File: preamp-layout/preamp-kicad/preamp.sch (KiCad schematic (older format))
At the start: 15 parts

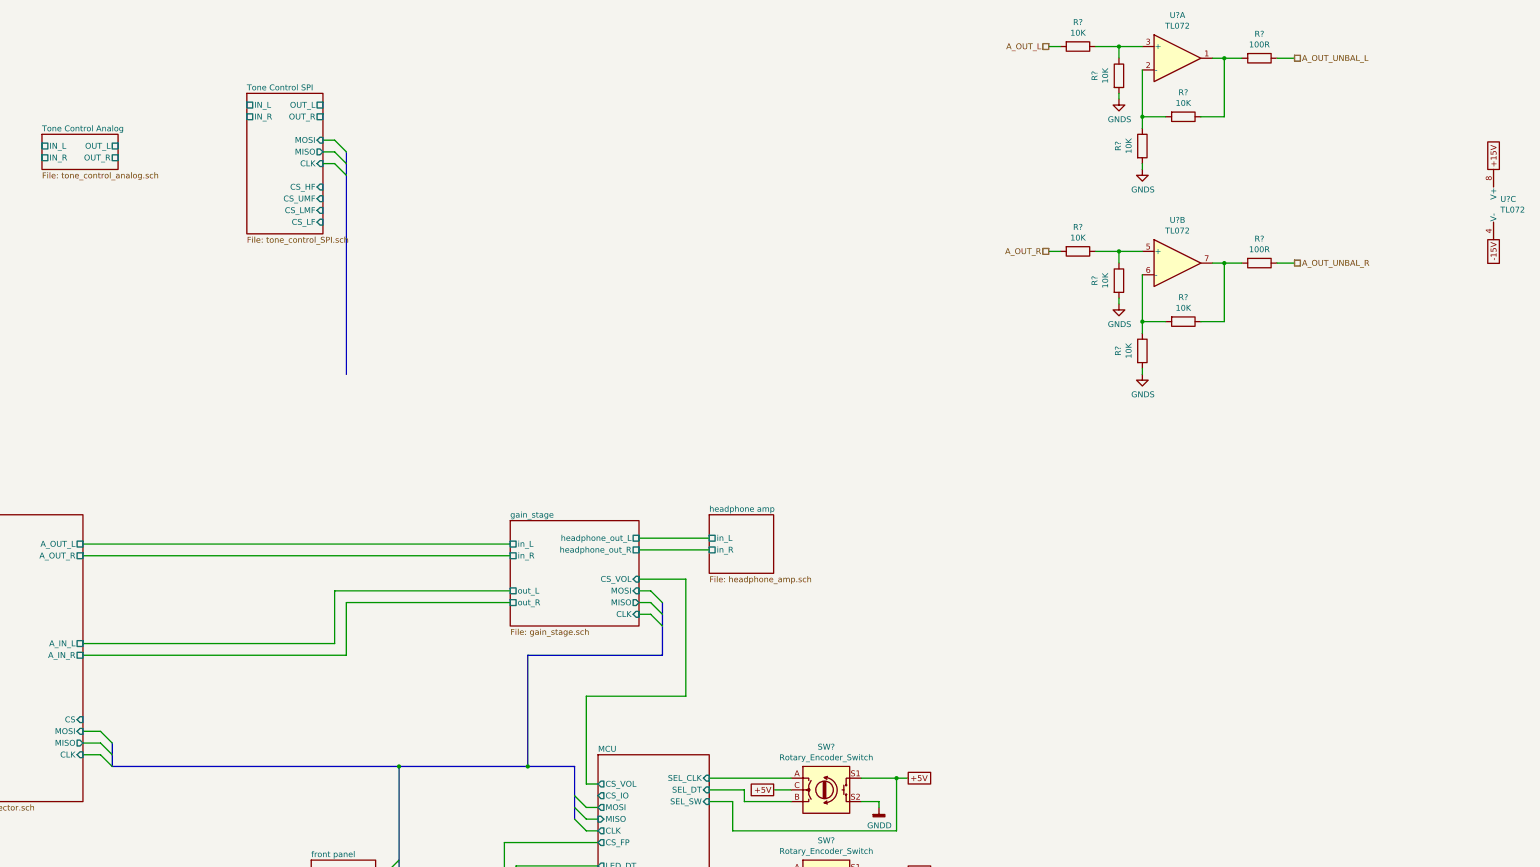
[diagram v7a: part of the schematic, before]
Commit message: Added preliminary gain stage
Gain stage added with choice of 6db or 12db gain. Cleaned up Gain stage IO pins on preamp sheet. Broke out volume ctrl to its own board, updated accordingly. Minor routing changes on preamp sheet.
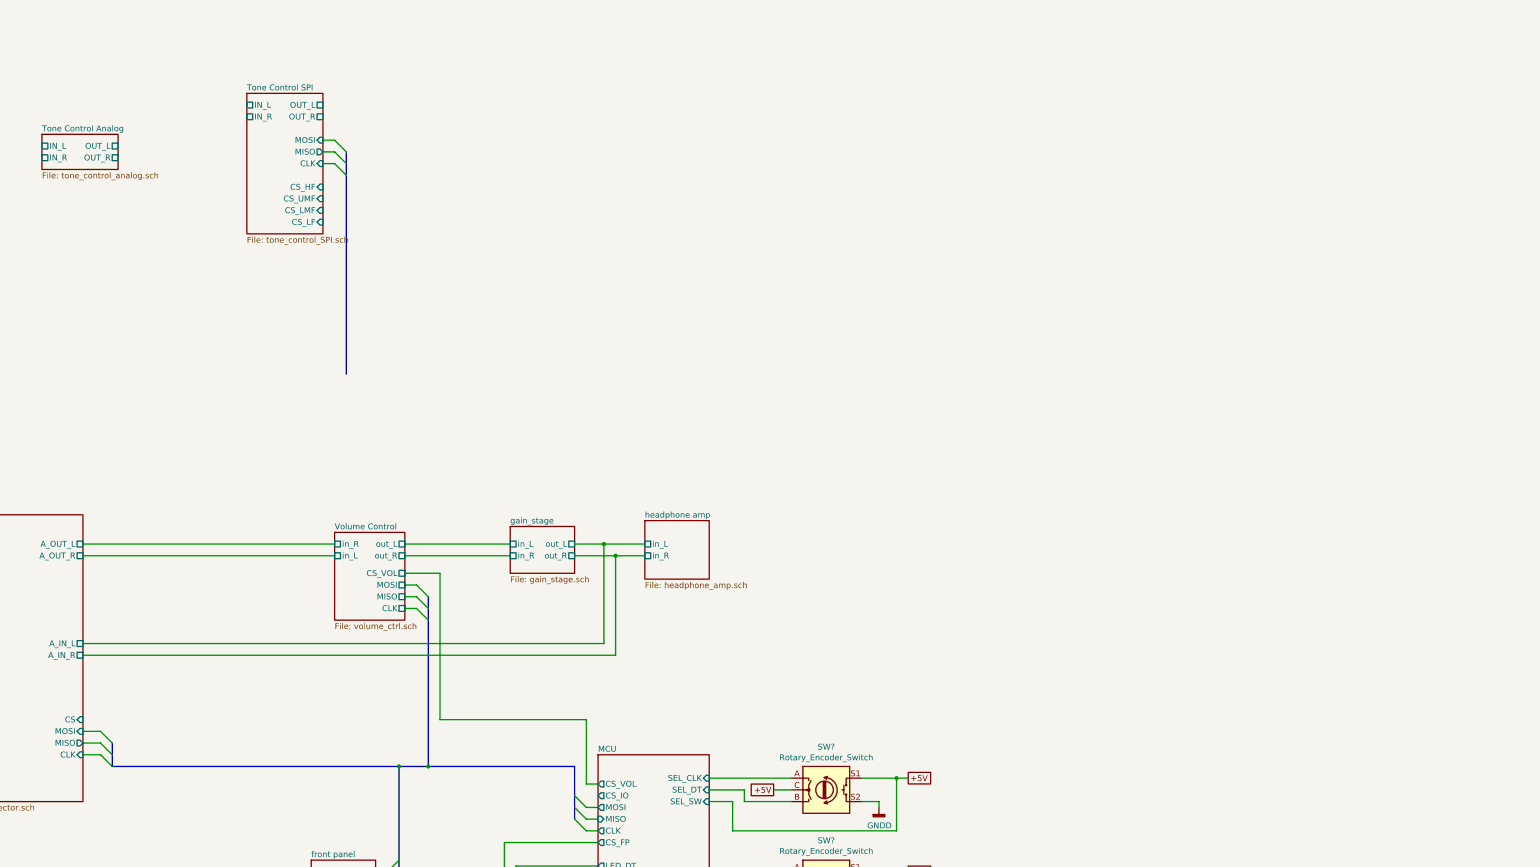
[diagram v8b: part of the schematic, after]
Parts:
- removed R? (x8): 10K, symbol Device:R
- removed R? (x2): 100R, symbol Device:R
- removed U? (x3): TL072, symbol Amplifier_Operational:TL072
